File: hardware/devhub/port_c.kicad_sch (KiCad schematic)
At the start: 18 parts, among them J1 USB-C, Q1 AO3400A, SW1 porta on/off, U1 TS3USB30E

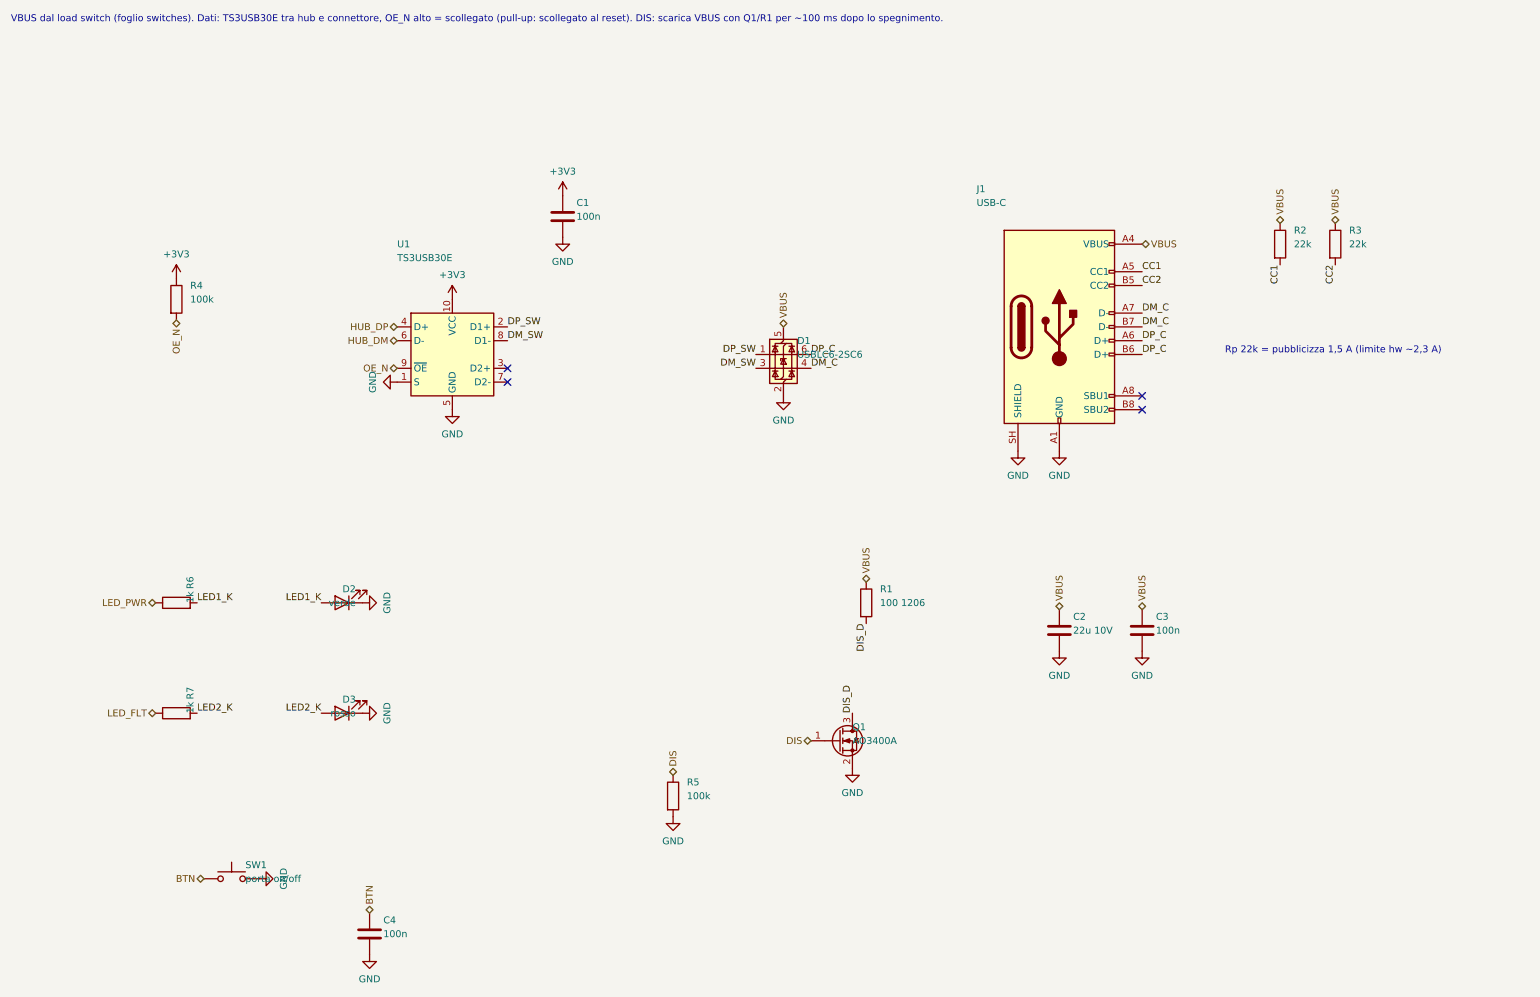
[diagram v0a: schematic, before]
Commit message: Schematic v0.2: hub reset supervisor, 1 A LDO, reorganized sheets, USB connectors and crystal
Functional changes:
- USB2517 RESET_N with pull-up and MCP120T-300 supervisor, wired-OR with
  the MCU (open-drain): resetting the MCU no longer resets the hub, so the
  ST DFU bootloader is reachable through it (D16/D17).
- 3.3 V LDO: AP7361C-33E (1 A, SOT-223) instead of AP2112K, which
  dissipated too much with the hub load.
- 74HC595 /OE on PB6 with pull-up: LEDs off until firmware enables them.
- Orange D93 instead of blue, USB-A bulk capacitance >= 120 uF, relay coil
  pinout fixed, snubbers marked DNP, Cliff FCR7350 banana jack footprints.
- D18: horizontal USB connectors, GCT USB4105-GF-A (USB-C) and Kycon
  KUSBX-AS1N-B (USB-A).
- D19: YXC X322524MOB4SI 24 MHz crystal (C_L 12 pF), 15 pF C0G load caps.

Layout: nearby parts wired directly, every net still explicitly named;
local labels inside sheets, global only across sheets, hierarchical for
ports. Files saved with KiCad 10.

Connectivity checked against the previous netlist, ERC clean.
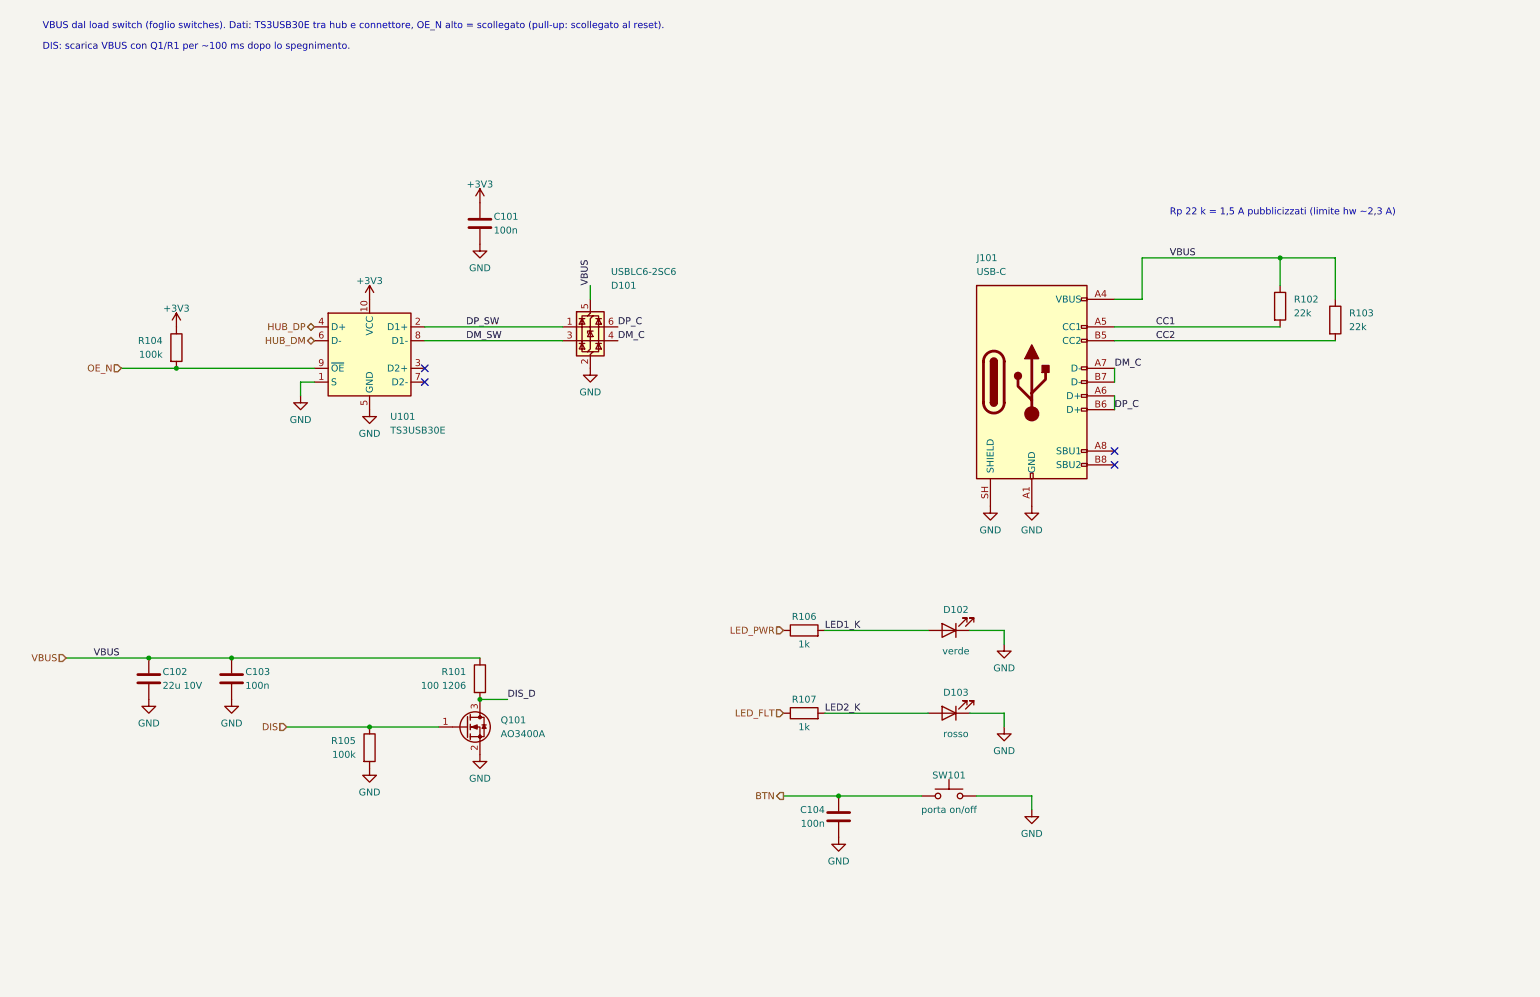
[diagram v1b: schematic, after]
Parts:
- removed C1, C3, C4: 100n, Capacitor_SMD:C_0603_1608Metric, symbol Device:C
- removed C2: 22u 10V, Capacitor_SMD:C_0805_2012Metric, symbol Device:C
- removed D1: USBLC6-2SC6, Package_TO_SOT_SMD:SOT-23-6, symbol Power_Protection:USBLC6-2SC6
- removed D2: verde, LED_SMD:LED_0805_2012Metric, symbol Device:LED
- removed D3: rosso, LED_SMD:LED_0805_2012Metric, symbol Device:LED
- removed J1: USB-C, Connector_USB:USB_C_Receptacle_GCT_USB4105-xx-A_16P_TopMnt_Horizontal, symbol Connector:USB_C_Receptacle_USB2.0_16P
- removed Q1: AO3400A, Package_TO_SOT_SMD:SOT-23, symbol Transistor_FET:AO3400A
- removed R1: 100 1206, Resistor_SMD:R_1206_3216Metric, symbol Device:R
- removed R2, R3: 22k, Resistor_SMD:R_0603_1608Metric, symbol Device:R
- removed R4, R5: 100k, Resistor_SMD:R_0603_1608Metric, symbol Device:R
- removed R6, R7: 1k, Resistor_SMD:R_0603_1608Metric, symbol Device:R
- removed SW1: porta on/off, Button_Switch_THT:SW_PUSH_6mm_H13mm, symbol Switch:SW_Push
- removed U1: TS3USB30E, Package_SO:TSSOP-10_3x3mm_P0.5mm, symbol Interface_USB:TS3USB30EDGSR
- added C101, C103, C104: 100n, Capacitor_SMD:C_0603_1608Metric, symbol Device:C
- added C102: 22u 10V, Capacitor_SMD:C_0805_2012Metric, symbol Device:C
- added D101: USBLC6-2SC6, Package_TO_SOT_SMD:SOT-23-6, symbol Power_Protection:USBLC6-2SC6
- added D102: verde, LED_SMD:LED_0805_2012Metric, symbol Device:LED
- added D103: rosso, LED_SMD:LED_0805_2012Metric, symbol Device:LED
- added J101: USB-C, Connector_USB:USB_C_Receptacle_GCT_USB4105-xx-A_16P_TopMnt_Horizontal, symbol Connector:USB_C_Receptacle_USB2.0_16P
- added Q101: AO3400A, Package_TO_SOT_SMD:SOT-23, symbol Transistor_FET:AO3400A
- added R101: 100 1206, Resistor_SMD:R_1206_3216Metric, symbol Device:R
- added R102, R103: 22k, Resistor_SMD:R_0603_1608Metric, symbol Device:R
- added R104, R105: 100k, Resistor_SMD:R_0603_1608Metric, symbol Device:R
- added R106, R107: 1k, Resistor_SMD:R_0603_1608Metric, symbol Device:R
- added SW101: porta on/off, Button_Switch_THT:SW_PUSH_6mm_H13mm, symbol Switch:SW_Push
- added U101: TS3USB30E, Package_SO:TSSOP-10_3x3mm_P0.5mm, symbol Interface_USB:TS3USB30EDGSR
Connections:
- net +3V3: now also C101.1, R104.1, U101.10 (VCC)
- net BTN: now also C104.1, SW101.1
- net CC1: now also J101.A5 (CC1), R102.2
- net CC2: now also J101.B5 (CC2), R103.2
- net DIS: now also Q101.1 (G), R105.1
- net DIS_D: now also Q101.3 (D), R101.2
- net DM_C: now also D101.4 (I/O2), J101.A7 (D-), J101.B7 (D-)
- net DM_SW: now also D101.3 (I/O2), U101.8 (D1-)
- net DP_C: now also D101.6 (I/O1), J101.A6 (D+), J101.B6 (D+)
- net DP_SW: now also D101.1 (I/O1), U101.2 (D1+)
- net GND: now also C101.2, C102.2, C103.2, C104.2, D101.2 (GND), D102.1 (K), D103.1 (K), J101.A1 (GND), J101.A12 (GND), J101.B1 (GND), J101.B12 (GND), J101.SH (SHIELD), Q101.2 (S), R105.2, SW101.2, U101.1 (S), U101.5 (GND)
- net HUB_DM: now also U101.6 (D-)
- net HUB_DP: now also U101.4 (D+)
- net LED1_K: now also D102.2 (A), R106.2
- net LED2_K: now also D103.2 (A), R107.2
- net LED_FLT: now also R107.1
- net LED_PWR: now also R106.1
- net OE_N: now also R104.2, U101.9 (~{OE})
- net VBUS: now also C102.1, C103.1, D101.5 (VBUS), J101.A4 (VBUS), J101.A9 (VBUS), J101.B4 (VBUS), J101.B9 (VBUS), R101.1, R102.1, R103.1
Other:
- note added: "DIS: scarica VBUS con Q1/R1 per ~100 ms dopo lo spegnimento."
- note added: "Rp 22 k = 1,5 A pubblicizzati (limite hw ~2,3 A)"
- note added: "VBUS dal load switch (foglio switches). Dati: TS3USB30E tra hub e connettore, OE_N alto = scollegato (pull-up: scollegato al reset)."
- note removed: "Rp 22k = pubblicizza 1,5 A (limite hw ~2,3 A)"
- note removed: "VBUS dal load switch (foglio switches). Dati: TS3USB30E tra hub e connettore, OE_N alto = scollegato (pull-up: scollegato al reset). DIS: scarica VBUS con Q1/R1 per ~100 ms dopo lo spegnimento."

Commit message: Lab-use protection: TPS259470A input eFuse, PI3USB4002A data switches; AGENTS.md
Power input (D20, D21):
- TPS259470A eFuse after the shunt: trips above 5.84 V and below 4.0 V,
  zener on EN to withstand up to 28 V, 3.5 A limit, ~5 ms soft start,
  auto-retry, FLT to the MCU on PB1.
- The shunt stays before the eFuse, so the INA3221 still measures the input
  voltage when the eFuse is off.

Ports (D22): PI3USB4002A instead of TS3USB30E. The connector side withstands
24 V and opens above 4.75 V, so a D+/D- short to VBUS on a board under test
no longer reaches the 3.3 V rail.

Symbols for both ICs added to the project library. AGENTS.md added: the
schematic is edited in KiCad or with targeted changes, never regenerated by
script. Sheets re-saved by KiCad.

Connectivity checked against the previous netlist, ERC clean.
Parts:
- added C106: 1u 25V, Capacitor_SMD:C_0805_2012Metric, symbol Device:C
- U101: value TS3USB30E -> PI3USB4002A; footprint Package_SO:TSSOP-10_3x3mm_P0.5mm -> (none); symbol Interface_USB:TS3USB30EDGSR -> devhub:PI3USB4002A
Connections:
- net DM_SW: now also U101.7 (C0-); no longer U101.8 (D1-)
- net DP_SW: now also U101.8 (C0+); no longer U101.2 (D1+)
- net GND: now also C106.2; no longer U101.1 (S)
- net HUB_DM: now also U101.2 (L0-); no longer U101.6 (D-)
- net HUB_DP: now also U101.1 (L0+); no longer U101.4 (D+)
- new net SW_REF: C106.1, U101.6 (REF)
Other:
- note added: "VBUS dal load switch (foglio switches). Dati: PI3USB4002A tra hub e connettore, OE_N (EN) alto = scollegato (pull-up: scollegato al reset); lato connettore tollera 24 V e si apre da solo sopra 4,75 V."
- note removed: "VBUS dal load switch (foglio switches). Dati: TS3USB30E tra hub e connettore, OE_N alto = scollegato (pull-up: scollegato al reset)."

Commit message: Review 02, R02-01: remove USBLC6 from downstream ports (D27)
Adds the electrical review 02 document.

The USBLC6 VBUS pin sat on the switched port VBUS: its internal diodes fed
current from the data lines into the supply (an "off" port at ~2.6 V with a
self-powered board) and routed data overvoltage to 5 V, bypassing the 24 V
tolerance of the PI3USB4002A. Downstream ESD protection is now the one
integrated in the switch (10 kV IEC); the upstream port keeps its USBLC6.

Connectivity checked, ERC clean.
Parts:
- removed D101: USBLC6-2SC6, Package_TO_SOT_SMD:SOT-23-6, symbol Power_Protection:USBLC6-2SC6
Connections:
- net DM_SW is gone; now on net DM_C: U101.7 (C0-)
- net DP_SW is gone; now on net DP_C: U101.8 (C0+)
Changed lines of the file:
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@@
 	(wire
 		(pts
-			(xy 116.84 66.04) (xy 116.84 63.5)
+			(xy 40.64 78.74) (xy 66.04 78.74)
 		)
 		(stroke
@@
 	(wire
 		(pts
-			(xy 40.64 78.74) (xy 66.04 78.74)
+			(xy 218.44 58.42) (xy 243.84 58.42)
 		)
 		(stroke
@@
 	(wire
 		(pts
-			(xy 218.44 58.42) (xy 243.84 58.42)
+			(xy 213.36 73.66) (xy 254 73.66)
 		)
 		(stroke
@@
 	(wire
 		(pts
-			(xy 213.36 73.66) (xy 254 73.66)
+			(xy 213.36 71.12) (xy 243.84 71.12)
 		)
 		(stroke
@@
 	(wire
 		(pts
-			(xy 213.36 71.12) (xy 243.84 71.12)
+			(xy 96.52 139.7) (xy 101.6 139.7)
 		)
 		(stroke
@@
 	(wire
 		(pts
-			(xy 96.52 139.7) (xy 101.6 139.7)
+			(xy 160.02 127) (xy 179.07 127)
 		)
 		(stroke
@@
 	(wire
 		(pts
-			(xy 160.02 127) (xy 179.07 127)
+			(xy 86.36 78.74) (xy 96.52 78.74)
 		)
 		(stroke
@@
 	(wire
 		(pts
-			(xy 86.36 78.74) (xy 96.52 78.74)
+			(xy 30.48 78.74) (xy 40.64 78.74)
 		)
 		(stroke
@@
 	(wire
 		(pts
-			(xy 30.48 78.74) (xy 40.64 78.74)
+			(xy 76.2 144.78) (xy 88.9 144.78)
 		)
 		(stroke
@@
 	(wire
 		(pts
-			(xy 76.2 144.78) (xy 88.9 144.78)
+			(xy 218.44 66.04) (xy 218.44 58.42)
 		)
 		(stroke
@@
 	(wire
 		(pts
-			(xy 218.44 66.04) (xy 218.44 58.42)
+			(xy 243.84 58.42) (xy 254 58.42)
 		)
 		(stroke
@@
 	(wire
 		(pts
-			(xy 243.84 58.42) (xy 254 58.42)
+			(xy 198.12 157.48) (xy 198.12 160.02)
 		)
 		(stroke
@@
 	(wire
 		(pts
-			(xy 198.12 157.48) (xy 198.12 160.02)
+			(xy 86.36 73.66) (xy 96.52 73.66)
 		)
 		(stroke
@@
 	(wire
 		(pts
-			(xy 86.36 73.66) (xy 111.76 73.66)
+			(xy 60.96 144.78) (xy 76.2 144.78)
 		)
 		(stroke
@@
 	(wire
 		(pts
-			(xy 60.96 144.78) (xy 76.2 144.78)
+			(xy 213.36 66.04) (xy 218.44 66.04)
 		)
 		(stroke
@@
 	(wire
 		(pts
-			(xy 213.36 66.04) (xy 218.44 66.04)
+			(xy 187.96 157.48) (xy 198.12 157.48)
 		)
 		(stroke
@@
 	(wire
 		(pts
-			(xy 187.96 157.48) (xy 198.12 157.48)
+			(xy 35.56 132.08) (xy 50.8 132.08)
 		)
 		(stroke
@@
 	(wire
 		(pts
-			(xy 35.56 132.08) (xy 50.8 132.08)
+			(xy 152.4 157.48) (xy 162.56 157.48)
 		)
 		(stroke
@@
 	(wire
 		(pts
-			(xy 152.4 157.48) (xy 162.56 157.48)
+			(xy 193.04 127) (xy 193.04 129.54)
 		)
 		(stroke
@@
 	(wire
 		(pts
-			(xy 193.04 127) (xy 193.04 129.54)
+			(xy 186.69 142.24) (xy 193.04 142.24)
 		)
 		(stroke
@@
 	(wire
 		(pts
-			(xy 186.69 142.24) (xy 193.04 142.24)
+			(xy 243.84 58.42) (xy 243.84 63.5)
 		)
 		(stroke
@@
 	(wire
 		(pts
-			(xy 243.84 58.42) (xy 243.84 63.5)
+			(xy 186.69 127) (xy 193.04 127)
 		)
 		(stroke
@@
 	(wire
 		(pts
-			(xy 186.69 127) (xy 193.04 127)
+			(xy 86.36 71.12) (xy 96.52 71.12)
 		)
 		(stroke
 			(width 0)
 			(type default)
-		)
-	)
-	(wire
-		(pts
-			(xy 86.36 71.12) (xy 111.76 71.12)
-		)
-		(stroke
-			(width 0)
-			(type default)
-		)
-	)
-	(label "VBUS"
-		(at 116.84 63.5 90)
-		(effects
-			(font
-				(size 1.27 1.27)
-			)
-			(justify left bottom)
 		)
 	)
@@
 		)
 	)
-	(label "DP_SW"
-		(at 93.98 71.12 0)
+	(label "DP_C"
+		(at 96.52 71.12 0)
 		(effects
 			(font
@@
 		)
 	)
-	(label "DM_C"
-		(at 121.92 73.66 0)
-		(effects
-			(font
-				(size 1.27 1.27)
-			)
-			(justify left bottom)
-		)
-	)
 	(label "CC1"
 		(at 220.98 71.12 0)
@@
 		)
 	)
-	(label "DM_SW"
-		(at 93.98 73.66 0)
+	(label "DM_C"
+		(at 96.52 73.66 0)
 		(effects
 			(font
@@
 	(label "VBUS"
 		(at 25.4 132.08 0)
-		(effects
-			(font
-				(size 1.27 1.27)
-			)
-			(justify left bottom)
-		)
-	)
-	(label "DP_C"
-		(at 121.92 71.12 0)
 		(effects
 			(font
@@
 	)
 	(symbol
-		(lib_id "power:GND")
-		(at 116.84 78.74 0)
-		(unit 1)
-		(body_style 1)
-		(exclude_from_sim no)
-		(in_bom yes)
-		(on_board yes)
-		(in_pos_files yes)
-		(dnp no)
-		(property "Reference" "#PWR1007"
-			(at 116.84 78.74 0)
-			(hide yes)
-			(show_name no)
-			(do_not_autoplace no)
-			(effects
-				(font
-					(size 1.27 1.27)
-				)
-			)
-		)
-		(property "Value" "GND"
-			(at 116.84 83.14 0)
-			(show_name no)
-			(do_not_autoplace no)
-			(effects
-				(font
-					(size 1.27 1.27)
-				)
-			)
-		)
-		(property "Footprint" ""
-			(at 116.84 78.74 0)
-			(hide yes)
-			(show_name no)
-			(do_not_autoplace no)
-			(effects
-				(font
-					(size 1.27 1.27)
-				)
-			)
-		)
-		(property "Datasheet" ""
-			(at 116.84 78.74 0)
-			(hide yes)
-			(show_name no)
-			(do_not_autoplace no)
-			(effects
-				(font
-					(size 1.27 1.27)
-				)
-			)
-		)
-		(property "Description" ""
-			(at 116.84 78.74 0)
-			(hide yes)
-			(show_name no)
-			(do_not_autoplace no)
-			(effects
-				(font
-					(size 1.27 1.27)
-				)
-			)
-		)
-		(pin "1"
-		)
-		(instances
-			(project "devhub"
-				(path "/af6ea7d8-d1ba-5fc6-aec8-abf514847630/8fa65214-18b0-5d08-bb37-cbf5f7730b77"
-					(reference "#PWR1007")
-					(unit 1)
-				)
-				(path "/af6ea7d8-d1ba-5fc6-aec8-abf514847630/ac9618ab-6be7-5849-9695-cfee880af1b2"
-					(reference "#PWR4007")
-					(unit 1)
-				)
-				(path "/af6ea7d8-d1ba-5fc6-aec8-abf514847630/ba1682d4-60b7-5c55-978d-7c8e62460e69"
-					(reference "#PWR2007")
-					(unit 1)
-				)
-				(path "/af6ea7d8-d1ba-5fc6-aec8-abf514847630/dc5a11f0-6d53-54ad-a59a-d93c35141960"
-					(reference "#PWR3007")
-					(unit 1)
-				)
-			)
-		)
-	)
-	(symbol
 		(lib_id "Connector:USB_C_Receptacle_USB2.0_16P")
 		(at 198.12 81.28 0)
@@
 					(unit 1)
 				)
-			)
-		)
-	)
-	(symbol
-		(lib_id "Power_Protection:USBLC6-2SC6")
-		(at 116.84 71.12 0)
-		(unit 1)
-		(body_style 1)
-		(exclude_from_sim no)
-		(in_bom yes)
-		(on_board yes)
-		(in_pos_files yes)
-		(dnp no)
-		(property "Reference" "D101"
-			(at 120.65 63.5 0)
-			(show_name no)
-			(do_not_autoplace no)
-			(effects
-				(font
-					(size 1.27 1.27)
-				)
-				(justify left)
-			)
-		)
-		(property "Value" "USBLC6-2SC6"
-			(at 120.65 60.96 0)
-			(show_name no)
-			(do_not_autoplace no)
-			(effects
-				(font
-					(size 1.27 1.27)
-				)
-				(justify left)
-			)
-		)
-		(property "Footprint" "Package_TO_SOT_SMD:SOT-23-6"
-			(at 116.84 71.12 0)
-			(hide yes)
-			(show_name no)
-			(do_not_autoplace no)
-			(effects
-				(font
-					(size 1.27 1.27)
-				)
-			)
-		)
-		(property "Datasheet" "https://www.st.com/resource/en/datasheet/usblc6-2.pdf"
-			(at 116.84 71.12 0)
-			(hide yes)
-			(show_name no)
-			(do_not_autoplace no)
-			(effects
-				(font
-					(size 1.27 1.27)
-				)
-			)
-		)
-		(property "Description" "Very low capacitance ESD protection diode, 2 data-line, SOT-23-6"
-			(at 116.84 71.12 0)
-			(hide yes)
-			(show_name no)
-			(do_not_autoplace no)
-			(effects
-				(font
-					(size 1.27 1.27)
-				)
-			)
-		)
-		(pin "1"
-		)
-		(pin "2"
-		)
-		(pin "3"
-		)
-		(pin "4"
-		)
-		(pin "5"
-		)
-		(pin "6"
-		)
-		(instances
-			(project "devhub"
-				(path "/af6ea7d8-d1ba-5fc6-aec8-abf514847630/8fa65214-18b0-5d08-bb37-cbf5f7730b77"
-					(reference "D101")
-					(unit 1)
-				)
-				(path "/af6ea7d8-d1ba-5fc6-aec8-abf514847630/ac9618ab-6be7-5849-9695-cfee880af1b2"
-					(reference "D401")
-					(unit 1)
-				)
-				(path "/af6ea7d8-d1ba-5fc6-aec8-abf514847630/ba1682d4-60b7-5c55-978d-7c8e62460e69"
-					(reference "D201")
-					(unit 1)
-				)
-				(path "/af6ea7d8-d1ba-5fc6-aec8-abf514847630/dc5a11f0-6d53-54ad-a59a-d93c35141960"
-					(reference "D301")
-					(unit 1)
-				)

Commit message: Review 02, R02-03: USB-C ports advertise default USB current (Rp 56 k, D30)
RF-5 now distinguishes the advertised current from the hardware limit.
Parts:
- R102, R103: value 22k -> 56k
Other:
- note added: "Rp 56 k: annuncio standard USB (500 mA);"
- note added: "la porta non lo impone: limite hw ~2,3 A"
- note removed: "Rp 22 k = 1,5 A pubblicizzati (limite hw ~2,3 A)"
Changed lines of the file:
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@@
 		)
 	)
-	(text "Rp 22 k = 1,5 A pubblicizzati (limite hw ~2,3 A)"
+	(text "Rp 56 k: annuncio standard USB (500 mA);"
 		(exclude_from_sim no)
 		(at 223.52 50.8 0)
@@
 		)
 	)
+	(text "la porta non lo impone: limite hw ~2,3 A"
+		(exclude_from_sim no)
+		(at 223.52 53.34 0)
+		(effects
+			(font
+				(size 1.27 1.27)
+			)
+			(justify left bottom)
+		)
+	)
 	(junction
 		(at 243.84 58.42)
@@
 			)
 		)
-		(property "Value" "22k"
+		(property "Value" "56k"
 			(at 246.38 68.58 0)
 			(show_name no)
@@
 			)
 		)
-		(property "Value" "22k"
+		(property "Value" "56k"
 			(at 256.54 71.12 0)
 			(show_name no)
